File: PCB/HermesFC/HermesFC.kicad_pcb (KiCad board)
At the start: 4 copper layers, 62.8 x 57.8 mm, 72 parts, among them J1 Conn_01x04, J2 Screw_Terminal_01x02, J3 Conn_01x04, J4 Conn_01x04, J5 Conn_01x04, J6 Conn_01x06, J7 USB_B_Micro, Q1 AO3401A, U1 STM32F405RGTx, U2 AP63203WU, U3 USBLC6-2SC6, U4 MPU-6050, U5 ICM-20948, U6 LD39015M18R, U7 NTS0104PW, U8 BMP280, Y1 16Mhz

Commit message: update
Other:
- board text added: "github.com/aadilnaji"
- board text removed: "github.com/Ga1lileo"
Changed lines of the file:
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@@
 		)
 	)
-	(gr_text "github.com/Ga1lileo"
+	(gr_text "github.com/aadilnaji"
 		(at 189.225 59.025 0)
 		(layer "B.SilkS")

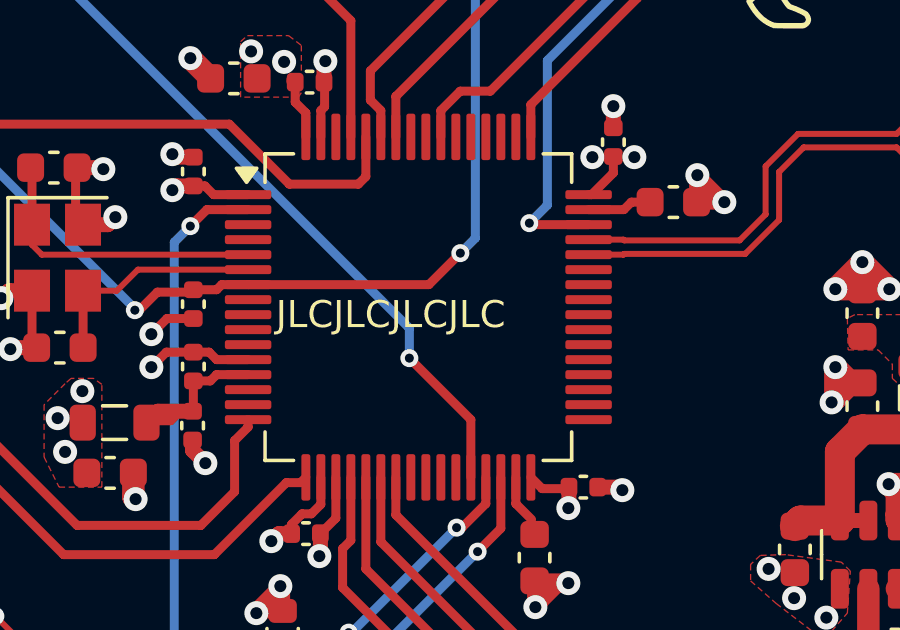
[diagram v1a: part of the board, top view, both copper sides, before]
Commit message: branch main design to create newer compact design
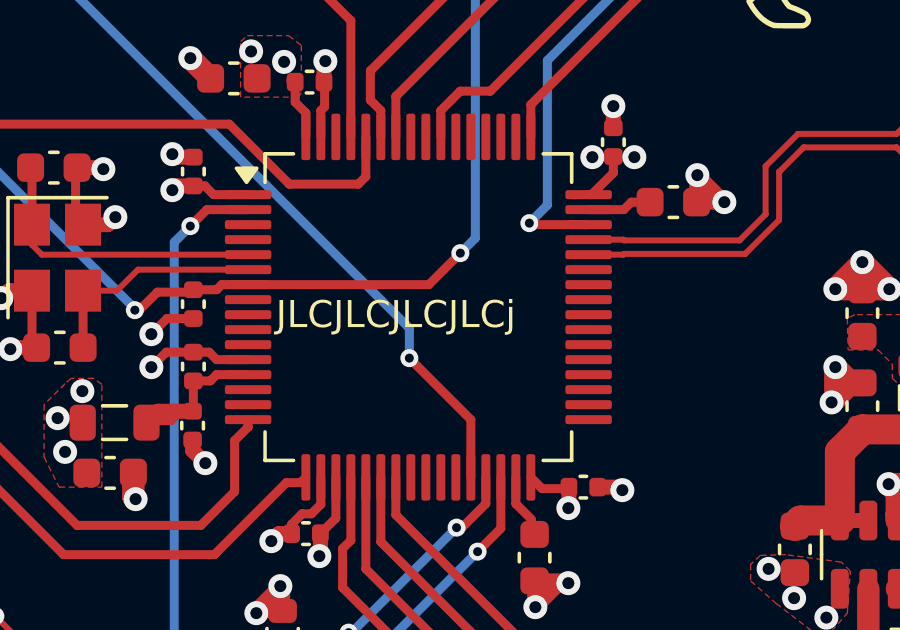
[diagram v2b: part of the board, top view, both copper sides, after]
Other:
- board text added: "JLCJLCJLCJLCj"
- board text removed: "JLCJLCJLCJLC"
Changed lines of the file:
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@@
 		)
 	)
-	(gr_text "JLCJLCJLCJLC\n"
+	(gr_text "JLCJLCJLCJLCj\n"
 		(at 166.85 71.275 0)
 		(layer "F.SilkS")

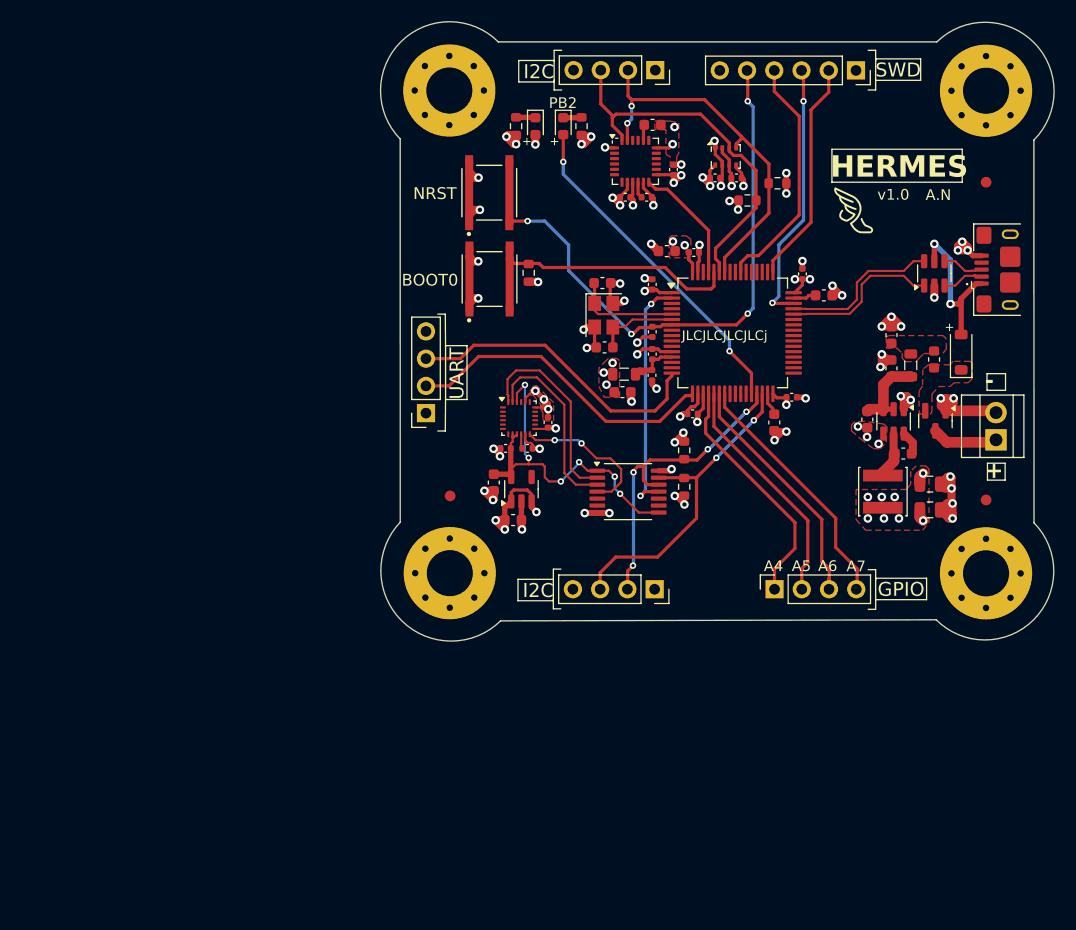
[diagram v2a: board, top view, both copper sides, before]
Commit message: update design to be more compact
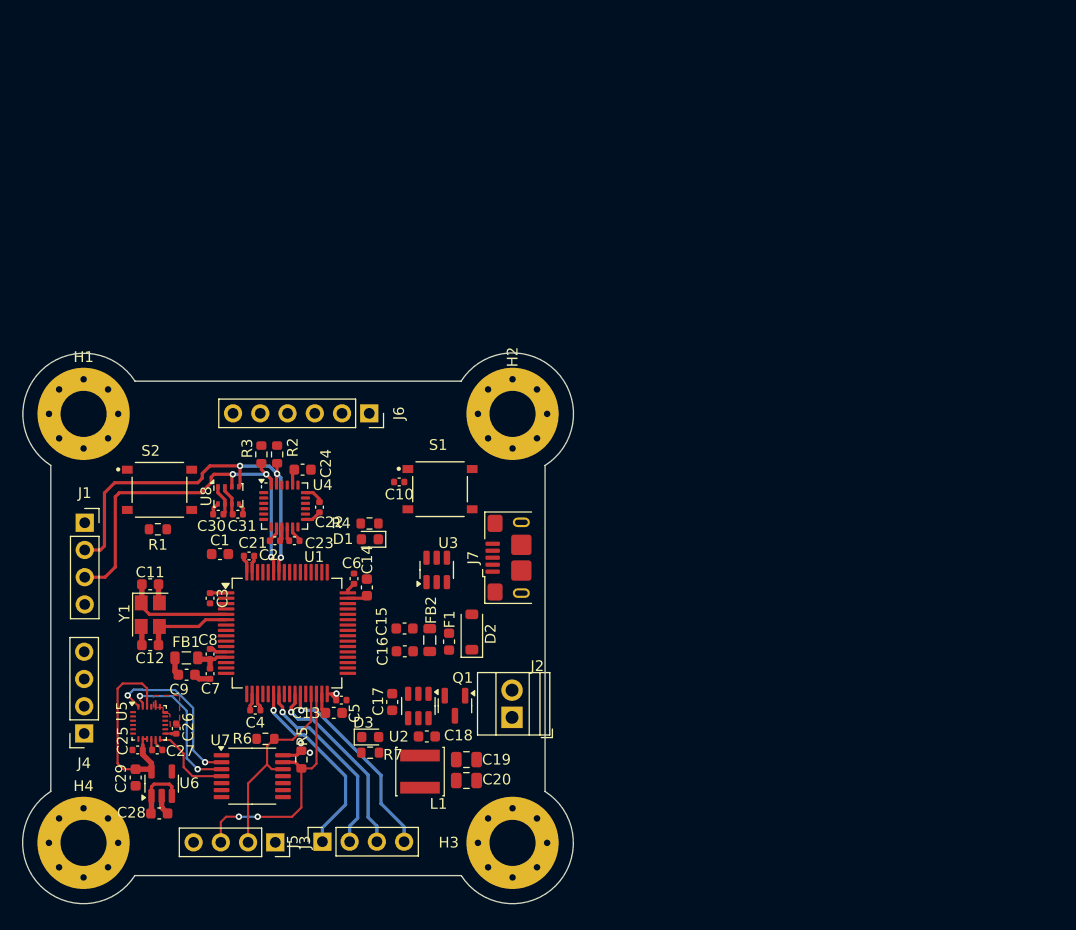
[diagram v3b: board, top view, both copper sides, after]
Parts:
- removed G***: LOGO, LOGO
- removed REF** (x3): Fiducial_1mm_Mask2mm, Fiducial:Fiducial_1mm_Mask2mm
- moved H4 87.8 mm to (111.1, 118.0), turned to 0 degrees
- moved H3 70.4 mm to (151.1, 118.0), turned to 0 degrees
- moved J1 67.9 mm to (111.2, 88.2), turned to 0 degrees
- moved C3 63.0 mm to (122.9, 95.2), turned to -90 degrees
- moved R7 60.0 mm to (137.8, 109.6), turned to 0 degrees
- moved D3 59.0 mm to (137.8, 108.2), turned to 0 degrees
- moved U8 56.1 mm to (124.6, 85.7)
- moved C31 56.1 mm to (125.5, 87.4)
- moved C30 55.9 mm to (123.6, 87.4)
- moved J6 55.5 mm to (137.7, 78.0)
- moved C4 54.3 mm to (127.1, 105.7), turned to 180 degrees
- moved U3 54.0 mm to (144.0, 92.6)
- moved H2 53.5 mm to (151.1, 78.0), turned to 0 degrees
- moved C5 53.1 mm to (135.1, 104.7)
- moved R2 53.1 mm to (129.1, 81.8), turned to -90 degrees
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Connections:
- J5 pad 1: MCU_PA4 -> TM3_CH1
- J5 pad 2: MCU_PA5 -> TM3_CH2
- J5 pad 3: MCU_PA6 -> TM3_CH3
- J5 pad 4: MCU_PA7 -> TM3_CH4
- U1 pad 14: unconnected-(U1-PA0-Pad14) -> ICM_INT_3v3
- U1 pad 2: ICM_INT_3v3 -> unconnected-(U1-PC13-Pad2)
- U1 pad 20: MCU_PA4 -> unconnected-(U1-PA4-Pad20)
- U1 pad 21: MCU_PA5 -> unconnected-(U1-PA5-Pad21)
- U1 pad 22: MCU_PA6 -> TM3_CH1
- U1 pad 23: MCU_PA7 -> TM3_CH2
- U1 pad 26: unconnected-(U1-PB0-Pad26) -> TM3_CH3
- U1 pad 27: unconnected-(U1-PB1-Pad27) -> TM3_CH4
- U1 pad 28: LED -> unconnected-(U1-PB2-Pad28)
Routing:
- net GND: track 119.9 -> 22.3 mm, vias 63 -> 0
- net /STM32/NRST: track 58.2 -> 0.00 mm, vias 4 -> 0
- net +3V3: track 66.1 -> 24.3 mm, vias 43 -> 3
- net LED: track 31.4 -> 0.00 mm, vias 2 -> 0
- net USART2_RX: track 29.8 -> 0.00 mm
- net USART2_TX: track 28.6 -> 0.00 mm
- net /STM32/BOOT0: track 27.6 -> 0.00 mm
- net SWDIO: track 25.1 -> 0.00 mm, vias 2 -> 0
- net MCU_PA7: track 23.6 -> 0.00 mm
- net SWO: track 22.6 -> 0.00 mm
- net MCU_PA4: track 22.6 -> 0.00 mm
- net MCU_PA6: track 22.5 -> 0.00 mm
- net ICM_INT_3v3: track 22.3 -> 0.00 mm, vias 2 -> 0
- net MCU_PA5: track 22.1 -> 0.00 mm
- net SWCLK: track 21.0 -> 0.00 mm
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- removed copper zone on F.Cu, net +3V3
- removed copper zone on F.Cu, net Net-(C15-Pad1)
- removed copper zone on F.Cu, net Net-(D2-K)
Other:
- board size 62.8 x 57.8 mm -> 51.4 x 51.3 mm
- board text removed: "+"
- board text removed: "-"
- board text removed: "03/2025"
- board text removed: "3V3"
- board text removed: "3v3"
- board text removed: "A.N"
- board text removed: "A4"
- board text removed: "A5"
- board text removed: "A6"
- board text removed: "A7"
- board text removed: "Aadil Naji"
- board text removed: "BOOT0"
- board text removed: "CLK"
- board text removed: "G"
- board text removed: "GPIO"
- board text removed: "HERMES"
- board text removed: "I2C"
- board text removed: "JLCJLCJLCJLCj"
- board text removed: "NRST"
- board text removed: "PB2"
- board text removed: "RST"
- board text removed: "RX"
- board text removed: "SCL"
- board text removed: "SDA"
- board text removed: "SWD"
- board text removed: "SWO"
- board text removed: "TX"
- board text removed: "UART"
- board text removed: "github.com/aadilnaji"
- board text removed: "v1.0"

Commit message: complete compact routing
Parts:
- moved C10 22.6 mm to (122.9, 98.5), turned to -90 degrees
- moved D1 3.27 mm to (137.8, 86.5)
- moved R4 3.27 mm to (137.8, 85.0)
- moved D3 2.80 mm to (136.5, 110.7)
- moved R7 2.80 mm to (136.5, 112.1)
- moved C15 0.96 mm to (140.5, 98.9)
- moved C16 0.96 mm to (140.6, 101.0)
- moved FB2 0.96 mm to (142.9, 100.0)
- moved F1 0.88 mm to (144.8, 100.1)
- moved U3 0.87 mm to (144.3, 91.8)
- moved D2 0.87 mm to (147.1, 99.2)
- moved C21 0.52 mm to (128.4, 89.9), turned to 0 degrees
- moved R5 0.26 mm to (131.4, 110.5)
- moved C1 0.22 mm to (124.0, 91.2)
- moved S1 0.18 mm to (144.1, 85.1)
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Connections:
- H1 pad 1: (no net) -> GND
- H2 pad 1: (no net) -> GND
- H3 pad 1: (no net) -> GND
- H4 pad 1: (no net) -> GND
- J6 pad 2: SWCLK -> SWDIO
- J6 pad 3: SWDIO -> SWCLK
- U1 pad 51: unconnected-(U1-PC10-Pad51) -> LED
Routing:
- net GND: track 22.3 -> 94.0 mm, vias 0 -> 62
- net /STM32/NRST: track 0.00 -> 49.4 mm, vias 0 -> 2
- net +3V3: track 24.3 -> 58.4 mm, vias 3 -> 39
- net /STM32/BOOT0: track 0.00 -> 23.9 mm
- net SWDIO: track 0.00 -> 19.0 mm
- net USART2_RX: track 0.00 -> 18.3 mm
- net VDDIO_1v8: track 19.1 -> 36.1 mm, vias 0 -> 4
- net USART2_TX: track 0.00 -> 16.3 mm
- net SWCLK: track 0.00 -> 15.6 mm
- net SWO: track 0.00 -> 15.3 mm, vias 0 -> 2
- net ICM_INT_3v3: track 0.00 -> 14.2 mm, vias 0 -> 2
- net +5V: track 0.00 -> 13.7 mm, vias 0 -> 2
- net IMU_INT: track 0.00 -> 12.0 mm, vias 0 -> 2
- net USB_D+: track 0.00 -> 11.3 mm
- net USB_D-: track 0.00 -> 11.3 mm
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- added copper zone on F.Cu, net +12V
- added copper zone on B.Cu, net +3V3
- added copper zone on F.Cu, net +3V3
- added copper zone on F.Cu, net /STM32/BUCK_IN
- added copper zone on F.Cu, net Net-(C15-Pad1)
- added copper zone on F.Cu, net Net-(D2-K)

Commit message: finalise silkscreen
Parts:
- added G***: LOGO, LOGO, F.Cu at (137.7, 90.4)
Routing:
- net GND: track 94.0 -> 111.4 mm, vias 62 -> 64
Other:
- board text added: "+"
- board text added: "+3.3"
- board text added: "-"
- board text added: "BOOT0"
- board text added: "CH1"
- board text added: "CH2"
- board text added: "CH3"
- board text added: "CH4"
- board text added: "CK"
- board text added: "DIO"
- board text added: "Hermes"
- board text added: "I2C"
- board text added: "I2C2"
- board text added: "NRST"
- board text added: "PC10"
- board text added: "PWM"
- board text added: "RX"
- board text added: "SCL"
- board text added: "SDA"
- board text added: "SWD"
- board text added: "TIM3"
- board text added: "TX"
- board text added: "UART"

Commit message: minor changes C18
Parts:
- C18: footprint Capacitor_SMD:C_0603_1608Metric -> Capacitor_SMD:C_0805_2012Metric
- moved C19 0.21 mm to (146.8, 110.5)
- moved C20 0.21 mm to (146.8, 112.4)
- moved L1 0.21 mm to (142.4, 111.6)
- moved C18 0.19 mm to (143.1, 108.3)
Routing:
- net /STM32/BUCK_SW: track 3.54 -> 2.13 mm
- added copper zone on F.Cu, net /STM32/BUCK_SW
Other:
- board text added: "Aadil Naji Hermes Flight Controller v1.0 github.com/aadilnaji"
- board text added: "HERMES"
- board text removed: "Hermes"

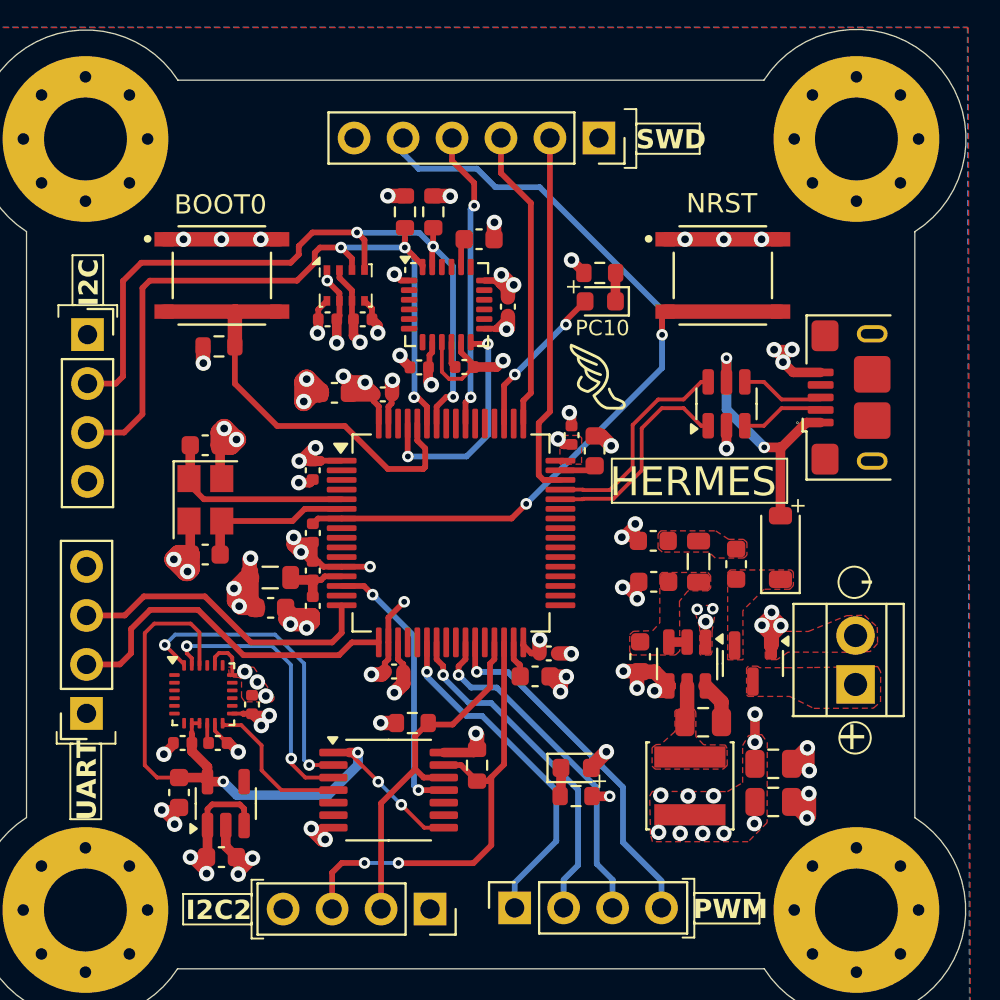
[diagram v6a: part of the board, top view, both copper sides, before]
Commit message: stitching between ground planes
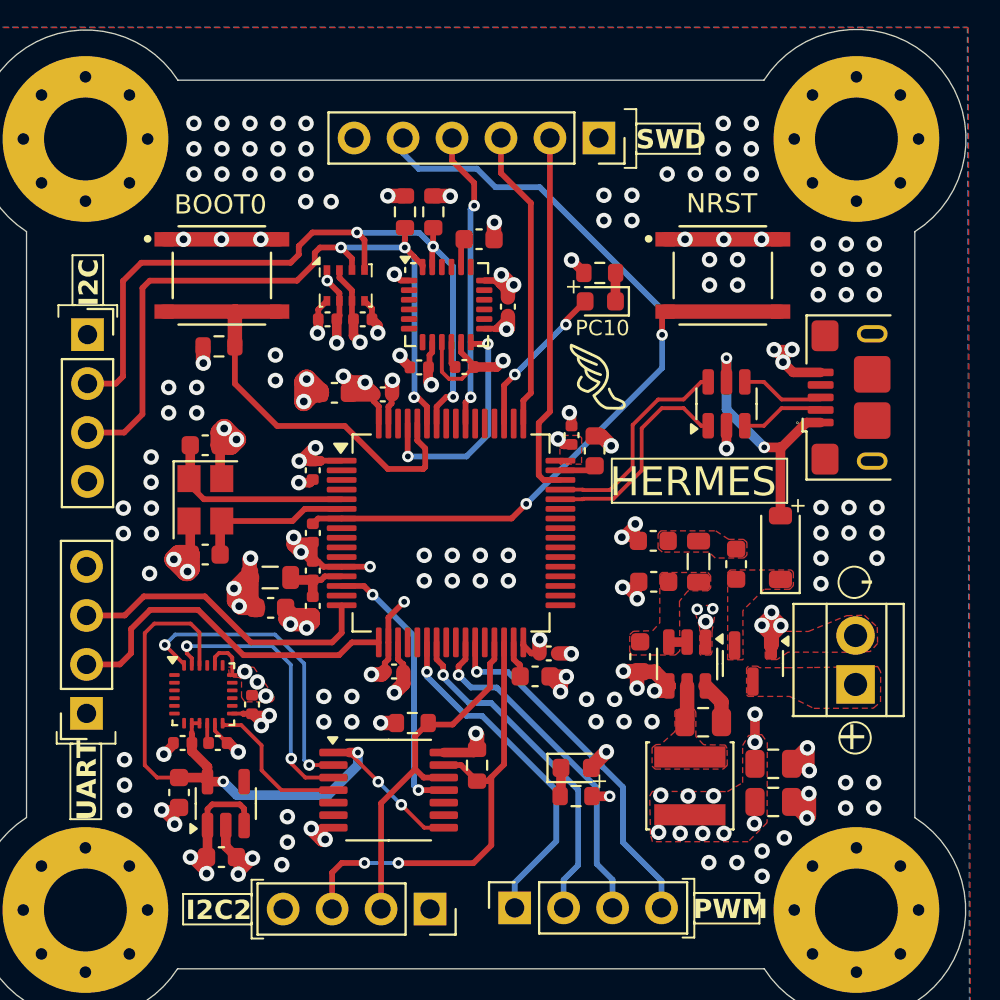
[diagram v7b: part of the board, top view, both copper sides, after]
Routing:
- net GND: vias 64 -> 160
